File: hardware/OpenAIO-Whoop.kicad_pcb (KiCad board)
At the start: 6 copper layers, 30.3 x 30.3 mm, 250 parts, among them J1 U.FL, J10 M3, J13 M4, J2 +, J20 LED, J21 5V, J22 BZ-, J23 CAM, J24 5V, J25 GND, J26 VHD, J27 GND, J28 TX0, J29 RX0, J3 -, J31 USB, J32 CAM, J33 GND, J4 M1, J7 M2, Q26 AP1606, Q27 BC857BM, Q28 AP1606, Q29 AGM210MAP, Q30 AGM210MAP, Q31 AGM210MAP, Q32 AGM210MAP, Q33 AGM210MAP, Q34 AGM210MAP, Q35 AGM210MAP, Q36 AGM210MAP, Q37 AGM210MAP, Q38 AGM210MAP, Q39 AGM210MAP, Q40 AGM210MAP, SW1 SKUBAAE010, U1 INA186A3, U10 RP2354A, U11 BMI270, U12 TPS7A2018, U13 PY25Q128HA-DFH-IR, U14 SN74LVC1G3157, U15 TLV7031, U16 ESP32-PICO-V3, U18 SX1281, U19 RTC6705, U2 TPS61022, U20 SE5004L, U21 LP5912-3.3, U22 LP5907-2.85, U4 LP5912-3.3, U6 EFM8BB51F16I, U7 EFM8BB51F16I, U8 EFM8BB51F16I, U9 EFM8BB51F16I, X1 12MHz, X3 52MHz TCXO, X4 8MHz 10pF

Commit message: Preserve owner schematic and board before final design review
Snapshot of the saved working design supplied for review.
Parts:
- removed C1, C2: 22uF, lib:C_0603_1608Metric_L
- removed C134: 4.7uF, lib:C_0201_0603Metric_L
- removed R1: 0.5mR 2W, lib:R_1206_Kelvin_4Pad_NetTie_HCS1206_L
- added R2: 0.5mR 2W, lib:R_1206_Kelvin_4Pad_NetTie_HCS1206_L, F.Cu at (102.0, 120.4)
- C100, C102, C105, C106, C107, C108, C109, C11, C111, C112, C114, C115, C116, C117, C118, C12, C123, C125, C128, C13, C42, C47, C48, C49, C50, C51, C52, C56, C58, C60, C61, C62, C66, C67, C68, C70, C94, D3, FB1, Q26, Q27, Q28, R43, R47, R48, R49, R54, R55, R64, R65, R66, R68, R71, R72, R81, R82, TP12, TP13, U11, U12, U15, U4: moved to F.Cu
- J1: moved to B.Cu
- moved C132 134.9 mm to (40.5, 125.8)
- moved C133 134.9 mm to (39.6, 124.0)
- moved C73 134.9 mm to (39.6, 127.7)
- moved C83 134.9 mm to (37.8, 122.6)
- moved C84 134.9 mm to (39.8, 130.0)
- moved C85 134.9 mm to (32.8, 122.5)
- moved C86 134.9 mm to (39.9, 131.5)
- moved C87 134.9 mm to (39.6, 130.8)
- moved C88 134.9 mm to (38.3, 128.1)
- moved C89 134.9 mm to (37.6, 124.2)
- moved C91 134.9 mm to (38.7, 123.5)
- moved R56 134.9 mm to (37.8, 123.4)
- moved R88 134.9 mm to (40.0, 125.0)
- moved SW1 134.9 mm to (42.0, 131.6)
- moved U18 134.9 mm to (38.8, 130.5)
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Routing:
- net GND: track 0.00 -> 13.1 mm
- net +BATT: track 0.00 -> 5.61 mm
- net /ESC2/B_COM: track 2.93 -> 6.80 mm, vias 3 -> 2
- net +1.1V: track 0.00 -> 3.64 mm
- net +3.3V: track 0.00 -> 3.58 mm
- net /ESC3/B_COM: track 2.99 -> 6.36 mm, vias 3 -> 2
- net /ESC3/NEUTRAL: track 0.00 -> 3.24 mm
- net /ESC2/NEUTRAL: track 0.00 -> 3.24 mm
- net /POWER/U2_SW: track 0.00 -> 2.94 mm
- net /RP2350A/VREG_LX: track 0.00 -> 2.90 mm
- net +5V_BST: track 0.00 -> 2.80 mm
- net /ESC2/B_PWM: track 3.80 -> 5.76 mm, vias 3 -> 2
- net /ESC3/B_PWM: track 3.80 -> 5.42 mm, vias 3 -> 2
- net /RP2350A/ADC_VBAT: track 0.00 -> 1.54 mm
- net /RP2350A/VREG_AVDD: track 0.00 -> 1.41 mm
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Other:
- board text added: "+"
- board text added: "-"
- board text removed: "STACKUP NextPCB 06101103-1080, 6L HDI 1+4+1, 1.0 mm, FR-4 Dk 4.2 L1 F.Cu 1 oz parts, RF 50R CPWG 0.105/0.15, hot loops, fan-out 1080 0.077 laser microvia L1-L2 0.10/0.25, in pad L2 In1 1 oz* solid GND plane, no tracks 1080 0.077 (* plated foil) L3 In2 1 oz signal layer, refs L2; no Analog / RF core 0.536 buried via L2-L5 0.15/0.35 (power 0.20/0.40) L4 In3 1 oz +BATT plane, refs L5; no Analog / RF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"

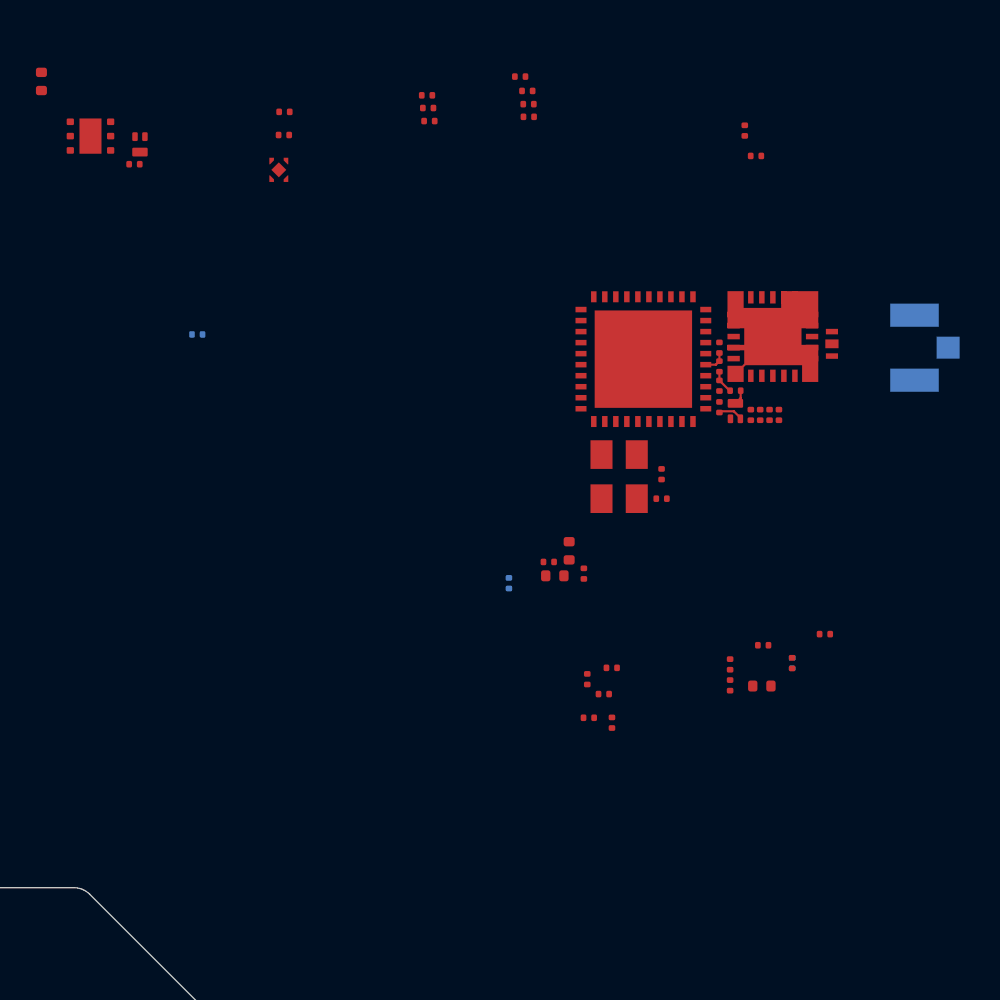
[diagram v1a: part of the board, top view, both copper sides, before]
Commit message: Correct Whoop schematic and prepare component library for routing
Add local BMI270 bypassing, improve regulator capacitance margin, isolate
bidirectional DShot supply domains, and correct PA reference accuracy.
Remove Q28/R11 with matching firmware polarity and retain the proven
OpenFC-Lite OSD topology. Correct the receiver LED bypass rail.

Synchronize PCB connectivity, verify component pins and land patterns,
and provide firmware bindings plus placement/layer guidance. Replace stale
manual BOM and interface plans with schematic-derived exports.

Validation: ERC 0, seven netlist checks, 48 footprint checks, 22 rule
behavior cases, and PCB schematic parity 0. The parked PCB retains layout
DRC findings and 499 unconnected items; no manufacturing or flight release.
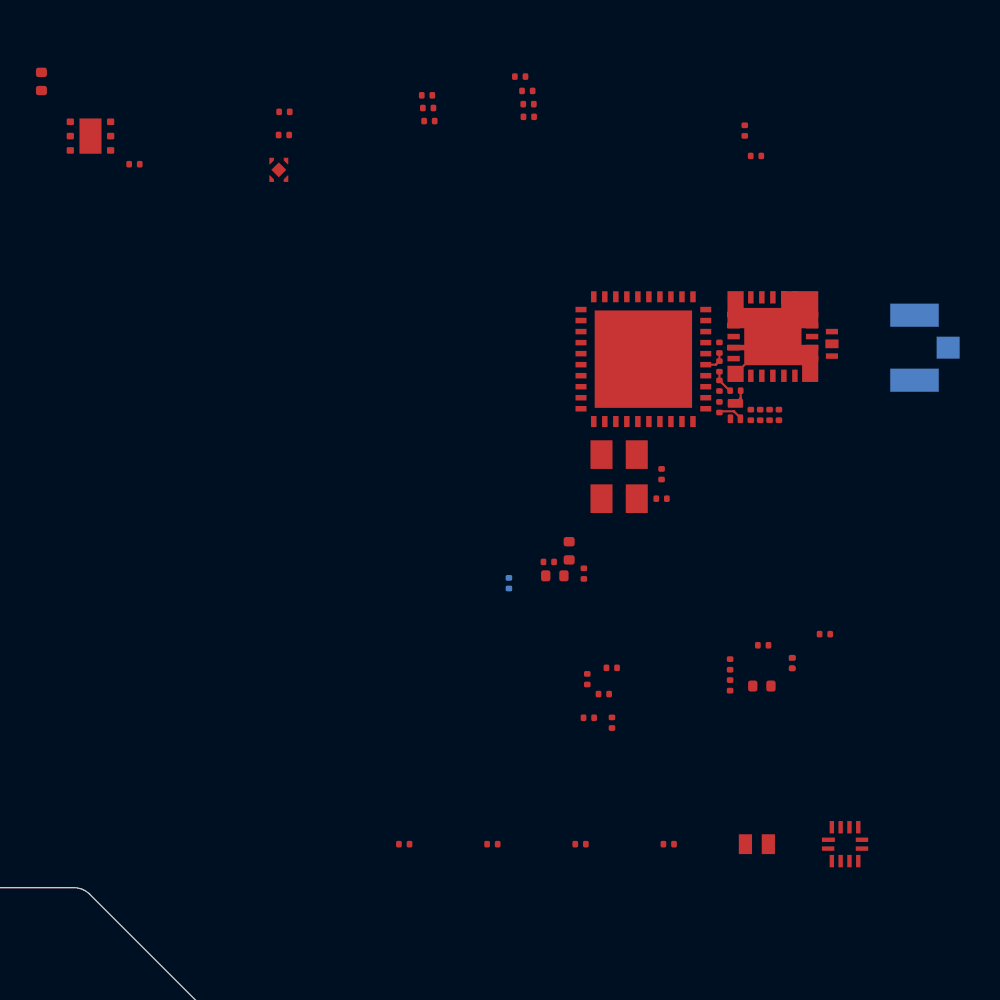
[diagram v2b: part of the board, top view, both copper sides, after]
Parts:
- removed Q28: AP1606, lib:DFN-3L_L1.0-W0.6-P0.65-BR_W
- removed R11: 2.4k, lib:R_0201_0603Metric_L
- added C137: 100nF, lib:C_0201_0603Metric_L, F.Cu at (133.4, 98.0)
- added C138: 100nF, lib:C_0201_0603Metric_L, F.Cu at (137.4, 98.0)
- added C143: 100nF, lib:C_0201_0603Metric_L, F.Cu at (141.4, 98.0)
- added C144: 100nF, lib:C_0201_0603Metric_L, F.Cu at (145.4, 98.0)
- added D11: MS2A40LDF, lib:DFN1610-2_L1.6-W1.0-P1.05-RD, F.Cu at (149.4, 98.0)
- added U24: FXMAR2104UMX, lib:Onsemi_UMLP-12_1.8x1.8mm_P0.4mm_FXMAR2104, F.Cu at (153.4, 98.0)
- C14, C61, C62: value 1uF -> 4.7uF
- C52: value 100nF -> 4.7uF
- R12, R19, R26, R33: value 2.4k -> 22R
- U22: value LP5907-2.85 -> TPS7A20285
- U4: value LP5912-3.3 -> TLV75733
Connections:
- net /RP2350A/U10_USB_DM renamed /RP2350A/U10_USB_D_N
- net /RP2350A/U10_USB_DP renamed /RP2350A/U10_USB_D_P
- C83 pad 1: +3.3V -> +5V
- R68 pad 2: /VTX/VTX_PWR_EN -> /HD_EN
- U10 pad 29: /MOTOR3 -> /RP2350A/MOTOR3_FC
- U10 pad 32: /MOTOR4 -> /RP2350A/MOTOR4_FC
- U10 pad 7: /MOTOR1 -> /RP2350A/MOTOR1_FC
- U10 pad 9: /MOTOR2 -> /RP2350A/MOTOR2_FC
- U21 pad 4: /VTX/VTX_PWR_EN -> /HD_EN
- U4 pad 3: unconnected-(U4-PG-Pad3) -> GND
- U4 pad 5: GND -> unconnected-(U4-NC-Pad5)

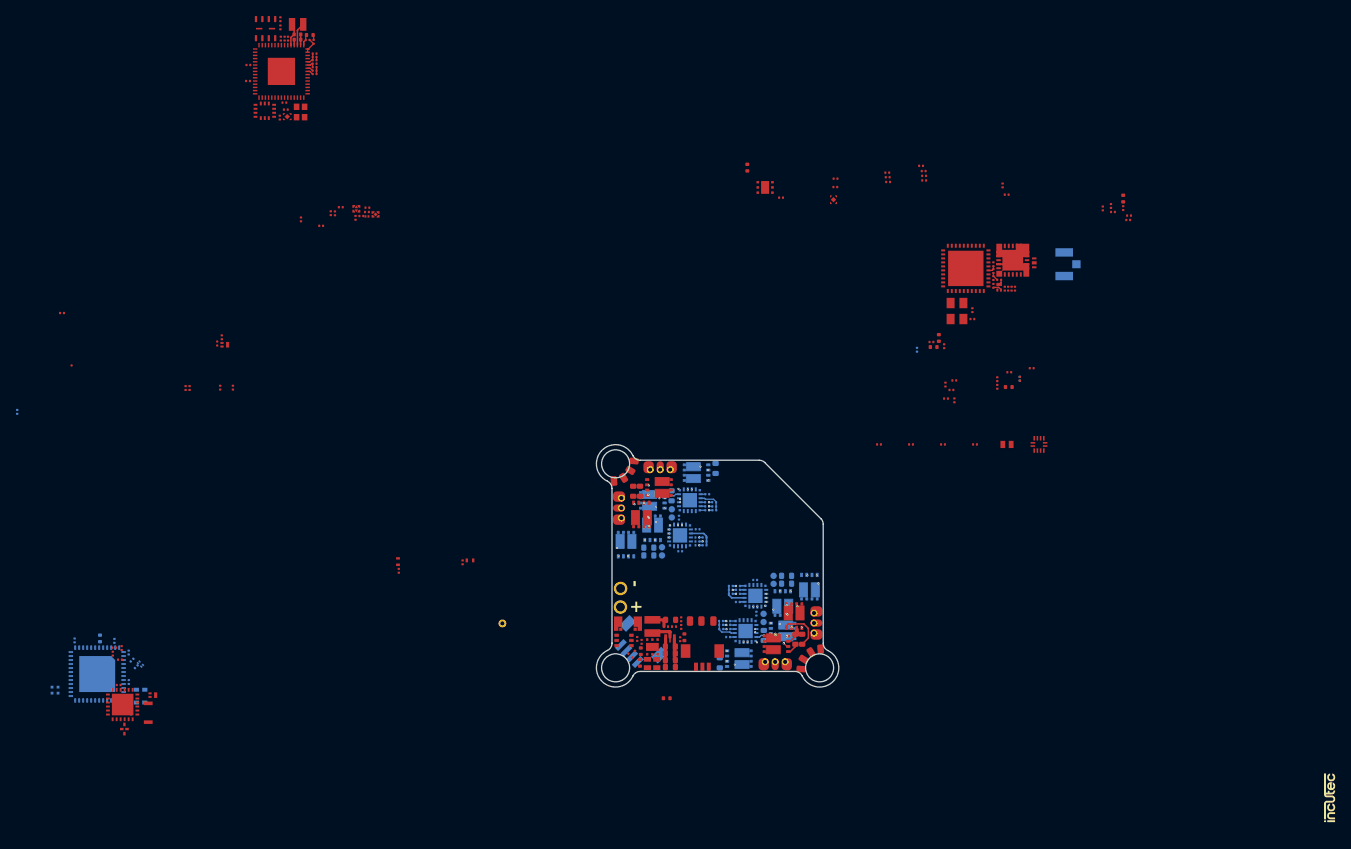
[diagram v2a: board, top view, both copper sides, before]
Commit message: Preserve owner schematic and placement edits before GPIO remap
Retain the saved layout, OSD bypass addition and component removals exactly
as received. This snapshot separates owner changes from the GPIO remap.
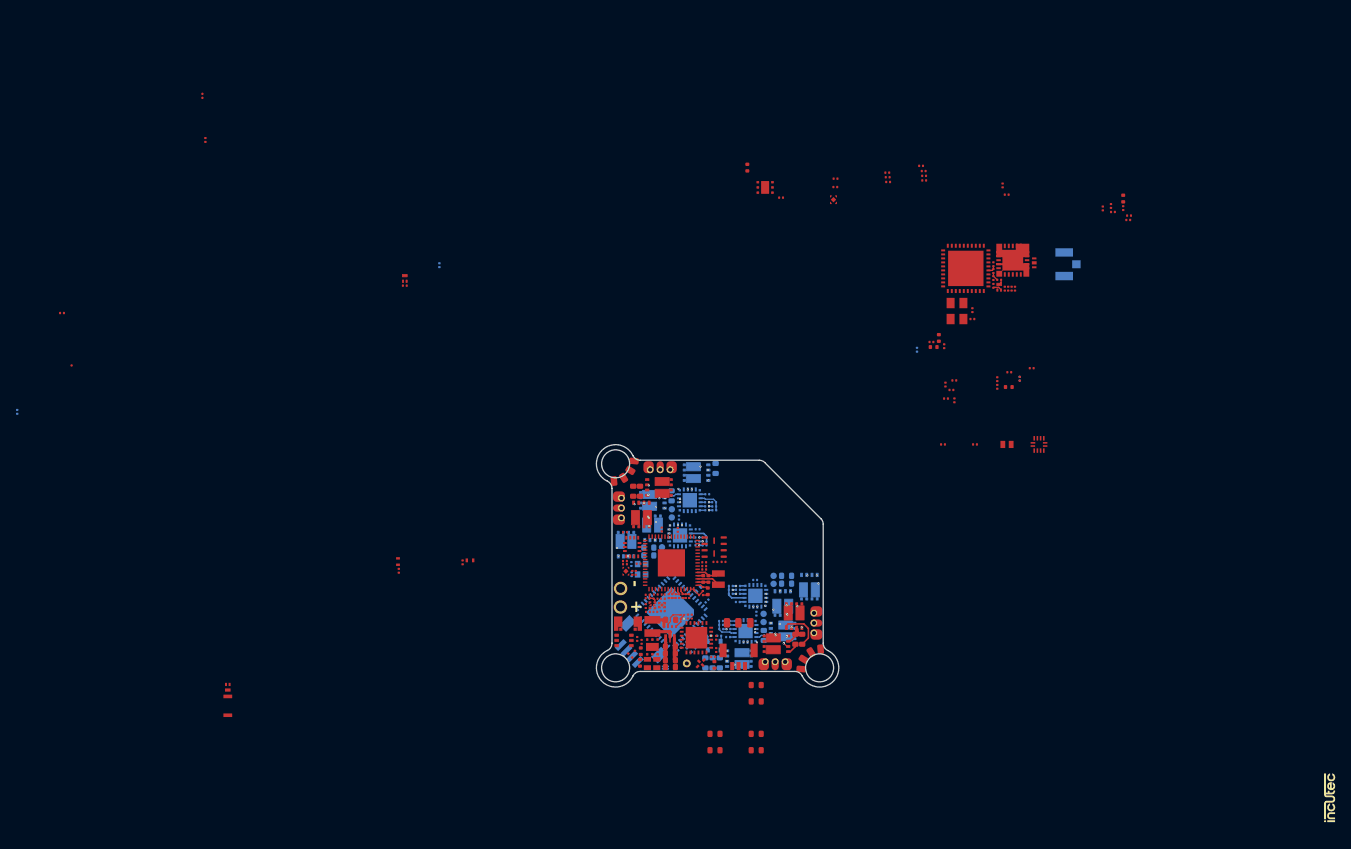
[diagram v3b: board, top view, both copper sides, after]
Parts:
- removed C13: 10uF, lib:C_0402_1005Metric_L
- removed C132, C133: 1.2pF, lib:C_0201_0603Metric_L
- removed R88: 0R, lib:R_0201_0603Metric_L
- added C22: 22uF, lib:C_0603_1608Metric_L, F.Cu at (118.0, 134.2)
- added C24: 22uF, lib:C_0603_1608Metric_L, B.Cu at (111.7, 125.3)
- added C28: 22uF, lib:C_0603_1608Metric_L, F.Cu at (112.9, 134.2)
- added C30: 22uF, lib:C_0603_1608Metric_L, F.Cu at (118.0, 128.1)
- added C34: 22uF, lib:C_0603_1608Metric_L, F.Cu at (118.0, 136.2)
- added C36: 22uF, lib:C_0603_1608Metric_L, B.Cu at (112.6, 125.3)
- added C40: 22uF, lib:C_0603_1608Metric_L, F.Cu at (112.9, 136.2)
- added C43: 22uF, lib:C_0603_1608Metric_L, F.Cu at (118.0, 130.2)
- added C71: 100nF, lib:C_0201_0603Metric_L, F.Cu at (106.3, 118.9)
- C42, C47, C70, C76, C89, R56, X1: moved to B.Cu
- C86, C87: moved to F.Cu
- moved R50 87.6 mm to (113.9, 112.7), turned to 0 degrees
- moved L2 87.0 mm to (113.3, 114.9), turned to -90 degrees
- moved C65 86.1 mm to (112.9, 112.7), turned to 0 degrees
- moved U13 85.7 mm to (112.8, 110.9), turned to 180 degrees
- moved C57 85.5 mm to (112.0, 116.4), turned to -90 degrees
- moved C56 85.3 mm to (112.0, 114.8), turned to -90 degrees
- moved R41 84.6 mm to (111.3, 116.1), turned to 90 degrees
- moved C44 84.4 mm to (111.1, 116.9), turned to 0 degrees
- moved C58 84.4 mm to (111.4, 114.8), turned to -90 degrees
- moved R43 84.3 mm to (111.5, 113.7), turned to 180 degrees
- moved R42 84.3 mm to (111.5, 113.2), turned to 0 degrees
- moved C45 84.2 mm to (111.5, 112.8), turned to 0 degrees
- moved R45 82.4 mm to (109.7, 117.0), turned to -90 degrees
- moved R46 81.8 mm to (109.2, 117.0), turned to 90 degrees
- moved C59 81.3 mm to (108.8, 117.0), turned to 90 degrees
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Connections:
- AE2 pad 1: /RX/RF_WIFI_ANT -> /RX/RF_WIFI
- AE2 pad 4: /RX/RF_WIFI_ANT -> /RX/RF_WIFI
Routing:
- net +5V_BST: track 2.80 -> 5.49 mm
- net /POWER/U2_FB: track 0.00 -> 1.87 mm
- net /VIDEO_IN: track 0.00 -> 1.53 mm
- net +3.3V: track 3.58 -> 4.32 mm
- net /RX/TCXO_OUT: track 0.00 -> 0.74 mm
- net /RX/XTA: track 0.00 -> 0.03 mm, vias 0 -> 1
- net GND: vias 0 -> 1

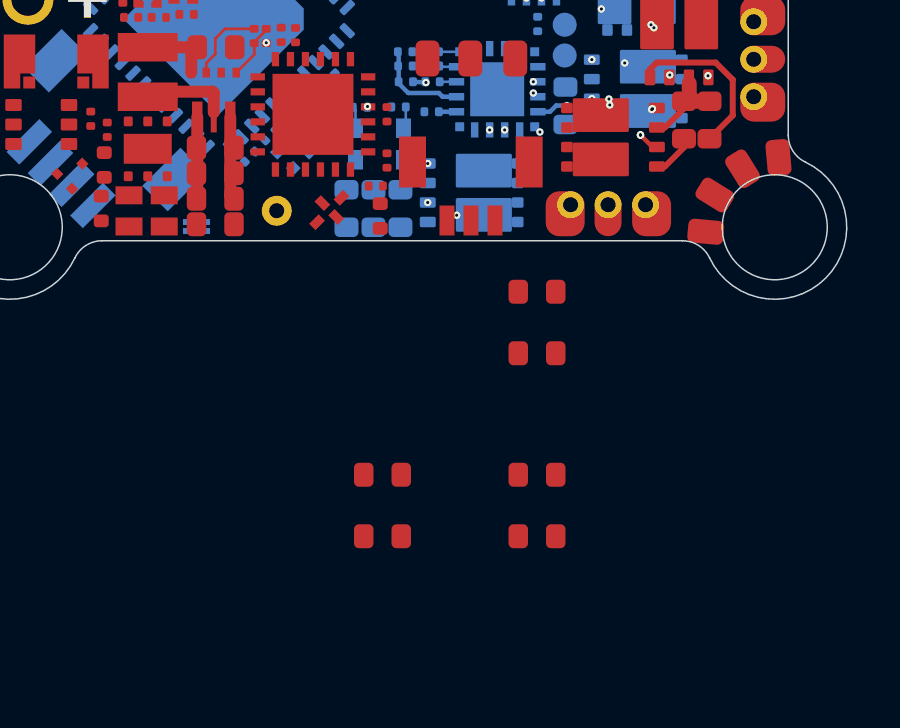
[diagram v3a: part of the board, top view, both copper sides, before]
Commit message: Group RP2354A interfaces around the placed peripherals
Map motors 1-4 to GPIO7/6/5/4 for U24 north-side fanout, move gyro INT
to GPIO10, and put CRSF UART1 on GPIO24/25 beside the ESP32. Keep the
gyro SPI pad order, flash, OSD, ADC and dedicated system pins. Move the
status LEDs, strip and beeper to the released pins.

Synchronize the target, project library, PCB nets and schematic print; add
a schematic-to-firmware IO check with mux and PIO constraints. Remove eight
stale PCB footprints already absent from the owner schematic. Preserve all
retained placement and copper geometry.

Validation: 28 GPIOs match, 7 netlist checks and 22 rule behavior cases pass,
Betaflight builds, independent circuit/PCB review passes. ERC retains four
owner warnings; parity is zero. Board layout has 282 DRC findings and
499 unconnected items. This is not a hardware-tested release.
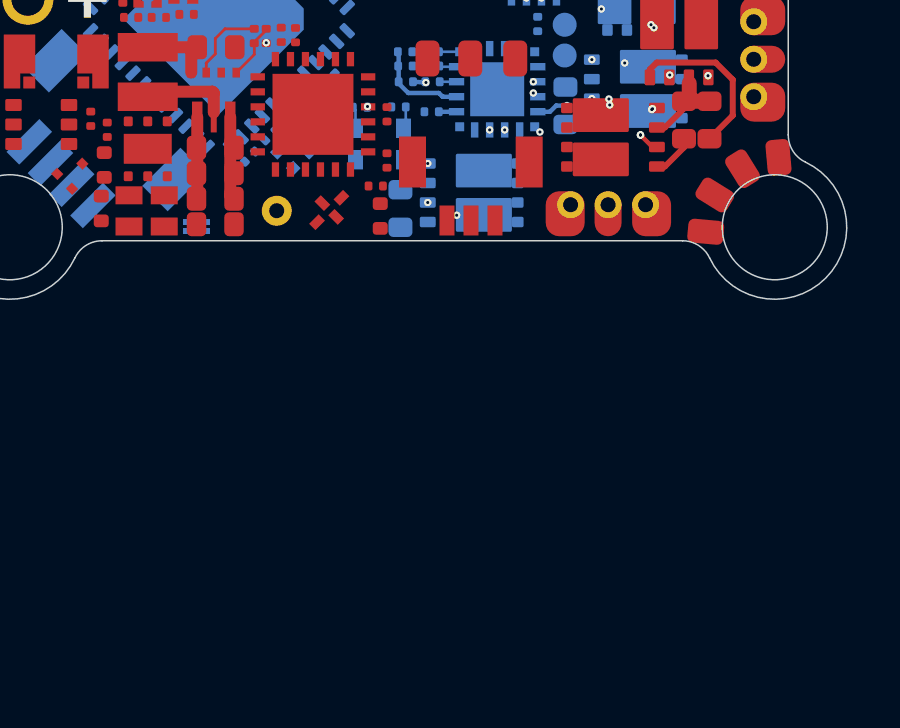
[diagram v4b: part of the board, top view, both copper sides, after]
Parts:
- removed C22, C24, C28, C30, C34, C36, C40, C43: 22uF, lib:C_0603_1608Metric_L
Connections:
- U10 pad 10: /GYRO_INT -> /RP2350A/MOTOR1_FC
- U10 pad 12: /UART1_TX -> /LED0
- U10 pad 13: /UART1_RX -> /LED1
- U10 pad 14: /LED0 -> /GYRO_INT
- U10 pad 29: /RP2350A/MOTOR3_FC -> /LED_STRIP
- U10 pad 32: /RP2350A/MOTOR4_FC -> /RP2350A/BEEPER
- U10 pad 36: /LED1 -> /UART1_TX
- U10 pad 37: /RP2350A/BEEPER -> /UART1_RX
- U10 pad 7: /RP2350A/MOTOR1_FC -> /RP2350A/MOTOR4_FC
- U10 pad 8: /LED_STRIP -> /RP2350A/MOTOR3_FC
